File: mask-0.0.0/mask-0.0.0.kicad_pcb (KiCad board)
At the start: 2 copper layers, 165 x 113 mm, 73 parts, among them SW1 SW_Push, SW10 SW_Push, SW11 SW_Push, SW12 SW_Push, SW13 SW_Push, SW13_1 SW_Push, SW14 SW_Push, SW15 SW_Push, SW16 SW_Push, SW17 SW_Push, SW18 SW_Push, SW19 SW_Push, SW2 SW_Push, SW20 SW_Push, SW20_1 SW_Push, SW21 SW_Push, SW22 SW_Push, SW23 SW_Push, SW24 SW_Push, SW25 SW_Push, SW26 SW_Push, SW27 SW_Push, SW27_1 SW_Push, SW28 SW_Push, SW29 SW_Push, SW3 SW_Push, SW30 SW_Push, SW31 SW_Push, SW32 SW_Push, SW33 SW_Push, SW34 SW_Push, SW35 SW_Push, SW4 SW_Push, SW5 SW_Push, SW6 SW_Push, SW7 SW_Push, SW8 SW_Push, SW9 SW_Push

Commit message: small changes
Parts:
- moved D31 0.71 mm to (48.0, 143.5), turned to 180 degrees
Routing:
- net Net-(D31-Pad2): track 0.00 -> 0.62 mm
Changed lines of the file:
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@@
   )
   (footprint "Diode_SMD_TopBottom:D_SOD-123_TopBottom" (layer "F.Cu")
-    (at 47.5 144)
+    (at 48 143.5 180)
     (descr "SOD-123")
     (tags "SOD-123")
@@
     (fp_line (start 0.25 -0.4) (end 0.25 0.4) (layer "F.Fab") (width 0.1))
     (fp_line (start -0.35 0) (end -0.35 -0.55) (layer "F.Fab") (width 0.1))
-    (pad "1" smd rect (at -1.65 0 180) (size 0.9 1.2) (layers "B.Cu" "B.Paste" "B.Mask")
+    (pad "1" smd rect (at -1.65 0) (size 0.9 1.2) (layers "B.Cu" "B.Paste" "B.Mask")
       (net 18 "/ROW4") (pinfunction "K"))
-    (pad "1" smd rect (at -1.65 0) (size 0.9 1.2) (layers "F.Cu" "F.Paste" "F.Mask")
+    (pad "1" smd rect (at -1.65 0 180) (size 0.9 1.2) (layers "F.Cu" "F.Paste" "F.Mask")
       (net 18 "/ROW4") (pinfunction "K"))
-    (pad "2" smd rect (at 1.65 0 180) (size 0.9 1.2) (layers "B.Cu" "B.Paste" "B.Mask")
+    (pad "2" smd rect (at 1.65 0) (size 0.9 1.2) (layers "B.Cu" "B.Paste" "B.Mask")
       (net 21 "Net-(D31-Pad2)") (pinfunction "A"))
-    (pad "2" smd rect (at 1.65 0) (size 0.9 1.2) (layers "F.Cu" "F.Paste" "F.Mask")
+    (pad "2" smd rect (at 1.65 0 180) (size 0.9 1.2) (layers "F.Cu" "F.Paste" "F.Mask")
       (net 21 "Net-(D31-Pad2)") (pinfunction "A"))
     (model "${KICAD6_3DMODEL_DIR}/Diode_SMD.3dshapes/D_SOD-123.wrl"
@@
   (gr_line (start 125.4 69.8) (end 125.4 65.3) (layer "User.1") (width 0.15))
   (gr_line (start 125.3988 145.9852) (end 125.3988 141.4852) (layer "User.1") (width 0.15))
+  (segment (start 39.980658 162.356748) (end 39.980658 162.980658) (width 0.25) (layer "F.Cu") (net 21))
 )

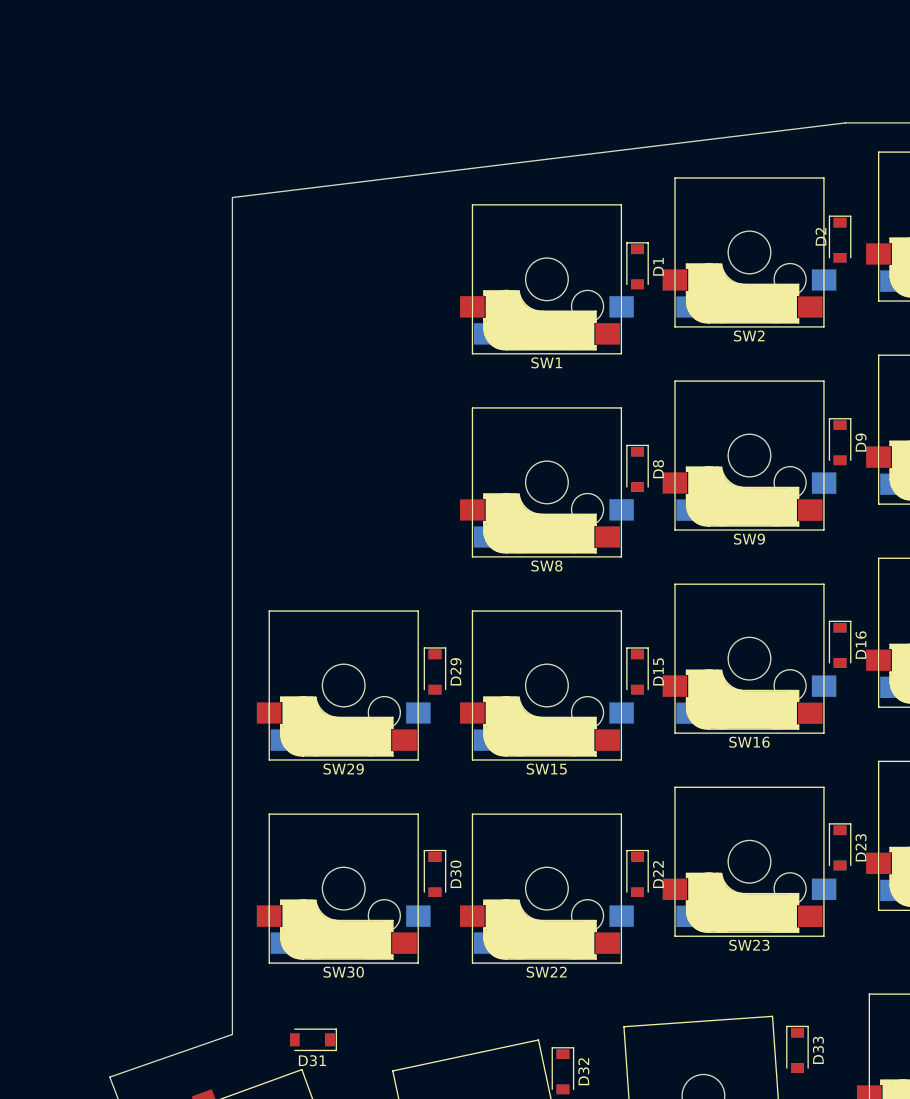
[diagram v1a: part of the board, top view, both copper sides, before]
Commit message: 0.0.0: create symbol/footprint for ble module, some schematic progress
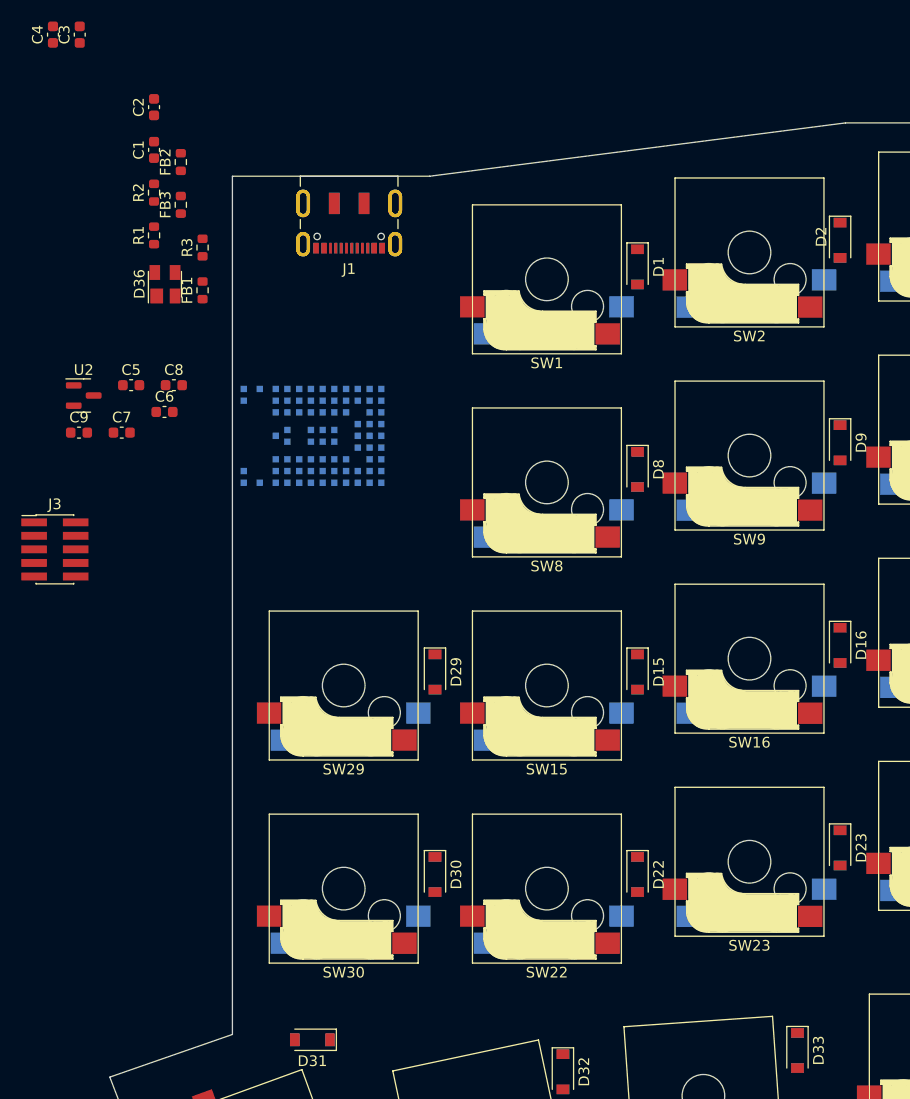
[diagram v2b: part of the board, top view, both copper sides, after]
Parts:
- added C1: 100nF, Capacitor_SMD:C_0603_1608Metric, F.Cu at (33.1, 60.0)
- added C2: 10nF, Capacitor_SMD:C_0603_1608Metric, F.Cu at (33.1, 56.0)
- added C3: 10nF, Capacitor_SMD:C_0603_1608Metric, F.Cu at (26.2, 49.2)
- added C4: 10pF, Capacitor_SMD:C_0603_1608Metric, F.Cu at (23.7, 49.2)
- added C5: 100nF, Capacitor_SMD:C_0603_1608Metric, F.Cu at (31.0, 82.1)
- added C6: 100nF, Capacitor_SMD:C_0603_1608Metric, F.Cu at (34.1, 84.6)
- added C7: 100nF, Capacitor_SMD:C_0603_1608Metric, F.Cu at (30.1, 86.5)
- added C8: 100nF, Capacitor_SMD:C_0603_1608Metric, F.Cu at (35.0, 82.1)
- added C9: 100nF, Capacitor_SMD:C_0603_1608Metric, F.Cu at (26.1, 86.5)
- added D36: PRTR5V0U2X, Package_TO_SOT_SMD:SOT-143, F.Cu at (34.2, 72.6)
- added FB1: 120R@550mA, Resistor_SMD:R_0603_1608Metric, F.Cu at (37.7, 73.2)
- added FB2: 120R@550mA, Resistor_SMD:R_0603_1608Metric, F.Cu at (35.7, 61.2)
- added FB3: 120R@550mA, Resistor_SMD:R_0603_1608Metric, F.Cu at (35.7, 65.2)
- added J1: USB_C_Receptacle_USB2.0, Connector_USB:USB_C_Receptacle_JAE_DX07S016JA1R1500, F.Cu at (51.5, 66.2)
- added J2: USB_C_Receptacle_USB2.0, Connector_USB:USB_C_Receptacle_JAE_DX07S016JA1R1500, B.Cu at (51.5, 66.2)
- added J3: Conn_ARM_JTAG_SWD_10, Connector_PinHeader_1.27mm:PinHeader_2x05_P1.27mm_Vertical_SMD, F.Cu at (23.9, 97.5)
- added R1: 5.11k, Resistor_SMD:R_0603_1608Metric, F.Cu at (33.1, 68.0)
- added R2: 5.11k, Resistor_SMD:R_0603_1608Metric, F.Cu at (33.1, 64.0)
- added R3: 10k, Resistor_SMD:R_0603_1608Metric, F.Cu at (37.7, 69.2)
- added U1: NORA-B10x, RF_Module_User:Ublox_NORA-B10x, B.Cu at (49.0, 86.8)
- added U2: MCP1703A-3302_SOT23, Package_TO_SOT_SMD:SOT-23, F.Cu at (26.5, 83.1)
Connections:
- net /COL0 renamed COL0
- net /COL1 renamed COL1
- net /COL2 renamed COL2
- net /COL3 renamed COL3
- net /COL4 renamed COL4
- net /COL5 renamed COL5
- net /COL6 renamed COL6
- net /ROW0 renamed ROW0
- net /ROW1 renamed ROW1
- net /ROW2 renamed ROW2
- net /ROW3 renamed ROW3
- net /ROW4 renamed ROW4
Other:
- outline, holes or cut-outs redrawn

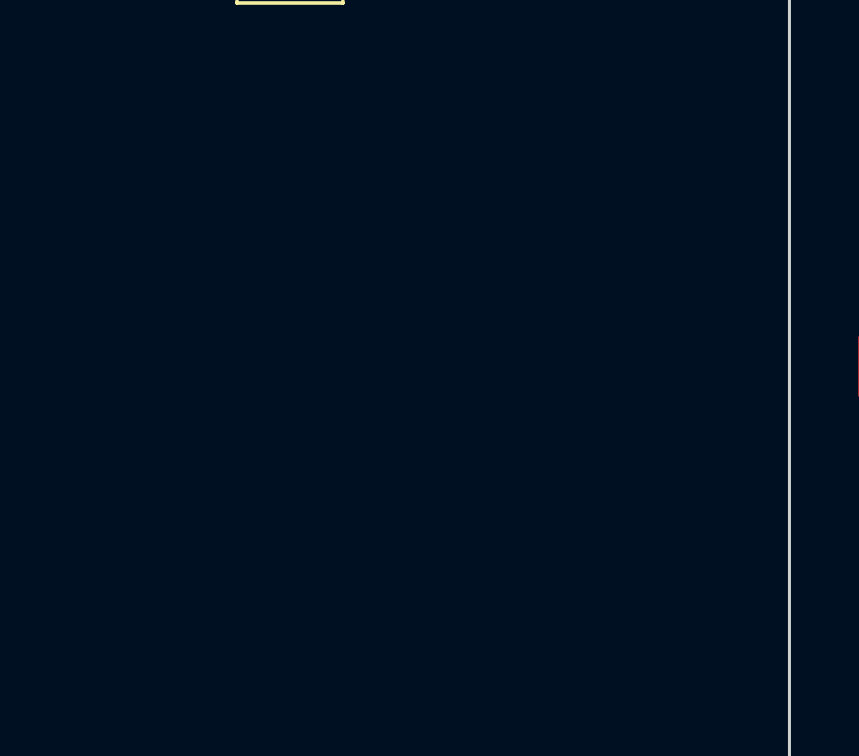
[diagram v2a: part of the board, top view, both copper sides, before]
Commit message: add leds (sk2812) and level converter
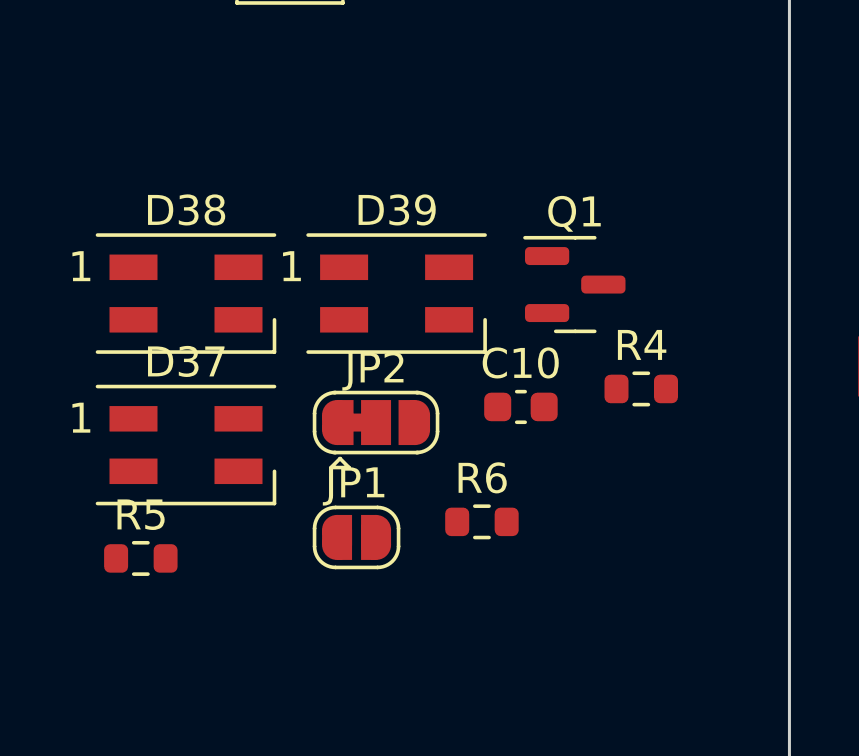
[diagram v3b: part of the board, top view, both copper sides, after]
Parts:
- added C10: 100nF, Capacitor_SMD:C_0603_1608Metric, F.Cu at (31.6, 114.2)
- added D37: SK6812MINI, LED_SMD:LED_SK6812MINI_PLCC4_3.5x3.5mm_P1.75mm, F.Cu at (20.4, 115.5)
- added D38: SK6812MINI, LED_SMD:LED_SK6812MINI_PLCC4_3.5x3.5mm_P1.75mm, F.Cu at (20.4, 110.4)
- added D39: SK6812MINI, LED_SMD:LED_SK6812MINI_PLCC4_3.5x3.5mm_P1.75mm, F.Cu at (27.4, 110.4)
- added JP1: Jumper_2_Open, Jumper:SolderJumper-2_P1.3mm_Open_RoundedPad1.0x1.5mm, F.Cu at (26.1, 118.5)
- added JP2: Jumper_3_Bridged12, Jumper:SolderJumper-3_P1.3mm_Bridged12_RoundedPad1.0x1.5mm, F.Cu at (26.7, 114.7)
- added Q1: IRLML2502, Package_TO_SOT_SMD:SOT-23, F.Cu at (33.4, 110.1)
- added R4: 10k, Resistor_SMD:R_0603_1608Metric, F.Cu at (35.6, 113.6)
- added R5: 10k, Resistor_SMD:R_0603_1608Metric, F.Cu at (18.9, 119.2)
- added R6: 10k, Resistor_SMD:R_0603_1608Metric, F.Cu at (30.2, 118.0)
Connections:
- J3 pad 1: unconnected-(J3-Pad1) -> +3V3
- J3 pad 10: unconnected-(J3-Pad10) -> RESET
- J3 pad 2: unconnected-(J3-Pad2) -> SWDIO
- J3 pad 3: Net-(J3-Pad3) -> GND
- J3 pad 4: unconnected-(J3-Pad4) -> SWDCLK
- J3 pad 5: Net-(J3-Pad3) -> GND
- J3 pad 6: unconnected-(J3-Pad6) -> SWO
- J3 pad 9: unconnected-(J3-Pad9) -> GND
- U1 pad B3: unconnected-(U1-PadB3) -> SWO
- U1 pad H2: unconnected-(U1-PadH2) -> SWDIO
- U1 pad J2: unconnected-(U1-PadJ2) -> SWDCLK
- U1 pad J3: unconnected-(U1-PadJ3) -> RESET

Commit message: udpate routing
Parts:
- removed the C1 at (33.1, 60.0)
- removed the C7 at (30.1, 86.5)
- removed the C8 at (35.0, 82.1)
- added C5: 100nF, Capacitor_SMD:C_0603_1608Metric, B.Cu at (42.3, 71.4)
- added D2: SK6812MINI, LED_SMD:LED_SK6812MINI_PLCC4_3.5x3.5mm_P1.75mm, B.Cu at (56.0, 73.3)
- added D4: SK6812MINI, LED_SMD:LED_SK6812MINI_PLCC4_3.5x3.5mm_P1.75mm, B.Cu at (56.0, 69.2)
- added D6: SK6812MINI, LED_SMD:LED_SK6812MINI_PLCC4_3.5x3.5mm_P1.75mm, B.Cu at (56.0, 65.1)
- added J1: Conn_02x05_Counter_Clockwise, Connector:Tag-Connect_TC2050-IDC-NL_2x05_P1.27mm_Vertical, B.Cu at (54.1, 99.5)
- C1: renamed from C5; moved to B.Cu
- C2: renamed from C6; moved to B.Cu
- C3: renamed from C9; moved to B.Cu
- C4: renamed from C10; moved to B.Cu
- C6: renamed from C2; moved to B.Cu
- C7: renamed from C3; moved to B.Cu
- C8: renamed from C4; moved to B.Cu
- D42: renamed from D36; moved to B.Cu
- FB1, FB2, FB3, JP1, JP2, Q1, U2: moved to B.Cu
- J2: renamed from J3; moved to B.Cu
- R1: renamed from R4; moved to B.Cu
- R2: renamed from R5; moved to B.Cu
- R3: renamed from R6; moved to B.Cu
- R4: renamed from R1; moved to B.Cu
- R5: renamed from R2; moved to B.Cu
- R6: renamed from R3; moved to B.Cu
- moved R2 58.0 mm to (58.9, 77.3), turned to -90 degrees
- moved D1 55.2 mm to (56.0, 73.3)
- moved D3 54.4 mm to (56.0, 69.2)
- moved D5 53.6 mm to (56.0, 65.1)
- moved JP1 48.4 mm to (55.8, 80.3)
- moved R3 47.0 mm to (52.3, 76.5)
- moved JP2 43.5 mm to (52.5, 79.6), turned to -90 degrees
- moved Q1 39.9 mm to (56.0, 77.3), turned to 180 degrees
- moved C8 36.2 mm to (46.6, 77.3), turned to -90 degrees
- moved C7 35.6 mm to (48.1, 77.3), turned to -90 degrees
- moved C1 26.0 mm to (56.9, 85.0), turned to 90 degrees
- moved C6 25.8 mm to (50.7, 74.9), turned to 0 degrees
- moved J2 20.6 mm to (44.4, 98.8), turned to -90 degrees
- moved R4 19.5 mm to (52.1, 72.5), turned to -90 degrees
- moved R5 19.4 mm to (50.5, 72.5), turned to -90 degrees
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- renumbered D37 to D1, D22 to D10, D29 to D11, D2 to D12, D9 to D13, D16 to D14, D23 to D15, D30 to D16, D3 to D17, D10 to D18, D17 to D19, D24 to D20, D31 to D21, D4 to D22, D11 to D23, D18 to D24, D32 to D26, D5 to D27, D12 to D28, D19 to D29, D38 to D3, D26 to D30, D33 to D31, D6 to D32, D13 to D33, D20 to D34, D27 to D35, D34 to D36, D7 to D37, D14 to D38, D21 to D39, D28 to D40, D35 to D41, D39 to D5, D1 to D7, D15 to D9, J1 to J3, J2 to J4, SW30 to SW10, SW3 to SW11, SW10 to SW12, SW17 to SW13, SW24 to SW14, SW31 to SW15, SW4 to SW16, SW11 to SW17, SW25 to SW19, SW8 to SW2, SW32 to SW20, SW5 to SW21, SW12 to SW22, SW19 to SW23, SW26 to SW24, SW33 to SW25, SW6 to SW26, SW13 to SW27, SW20 to SW28, SW27 to SW29, SW15 to SW3, SW34 to SW30, SW7 to SW31, SW14 to SW32, SW21 to SW33, SW28 to SW34, SW22 to SW4, SW29 to SW5, SW2 to SW6, SW9 to SW7, SW16 to SW8, SW23 to SW9
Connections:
- D5 pad 1: unconnected-(D39-Pad1) -> Net-(D5-Pad1)
- J2 pad 9: GND -> unconnected-(J2-Pad9)
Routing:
- net GND: track 0.00 -> 28.2 mm, vias 0 -> 3
- net VDD_LED: track 0.00 -> 24.5 mm, vias 0 -> 1
- net /Usb/GND_USB: track 0.00 -> 20.2 mm
- net /Usb/CC1: track 0.00 -> 18.9 mm, vias 0 -> 3
- net /Usb/CC2: track 0.00 -> 17.2 mm, vias 0 -> 2
- net D-: track 0.00 -> 15.9 mm, vias 0 -> 1
- net /Usb/VUSB: track 0.00 -> 11.3 mm
- net D+: track 0.00 -> 10.8 mm, vias 0 -> 1
- net Net-(D3-Pad1): track 0.00 -> 8.95 mm, vias 0 -> 1
- net Net-(D1-Pad1): track 0.00 -> 8.95 mm, vias 0 -> 1
- net /Usb/USB_SHIELD: track 0.00 -> 6.06 mm
- net Net-(D5-Pad1): track 0.00 -> 3.50 mm, vias 0 -> 1
- net +5V: track 0.00 -> 2.36 mm
- net +3V3: track 0.00 -> 1.83 mm
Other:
- board text added: "SW29: - x 48,4 - y 115,35 D29: - x 59,5 - y 109"
